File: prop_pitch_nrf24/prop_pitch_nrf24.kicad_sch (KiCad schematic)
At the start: 54 parts, among them J1 LOAD1, J2 LOAD2, J3 AVR-UPDI-6, J4 SERVO2, J5 SERVO1, J6 SERIAL, Q1 MMSS8550, U1 ATtiny1616-M, U2 HX711, U3 TPS563208DDCR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

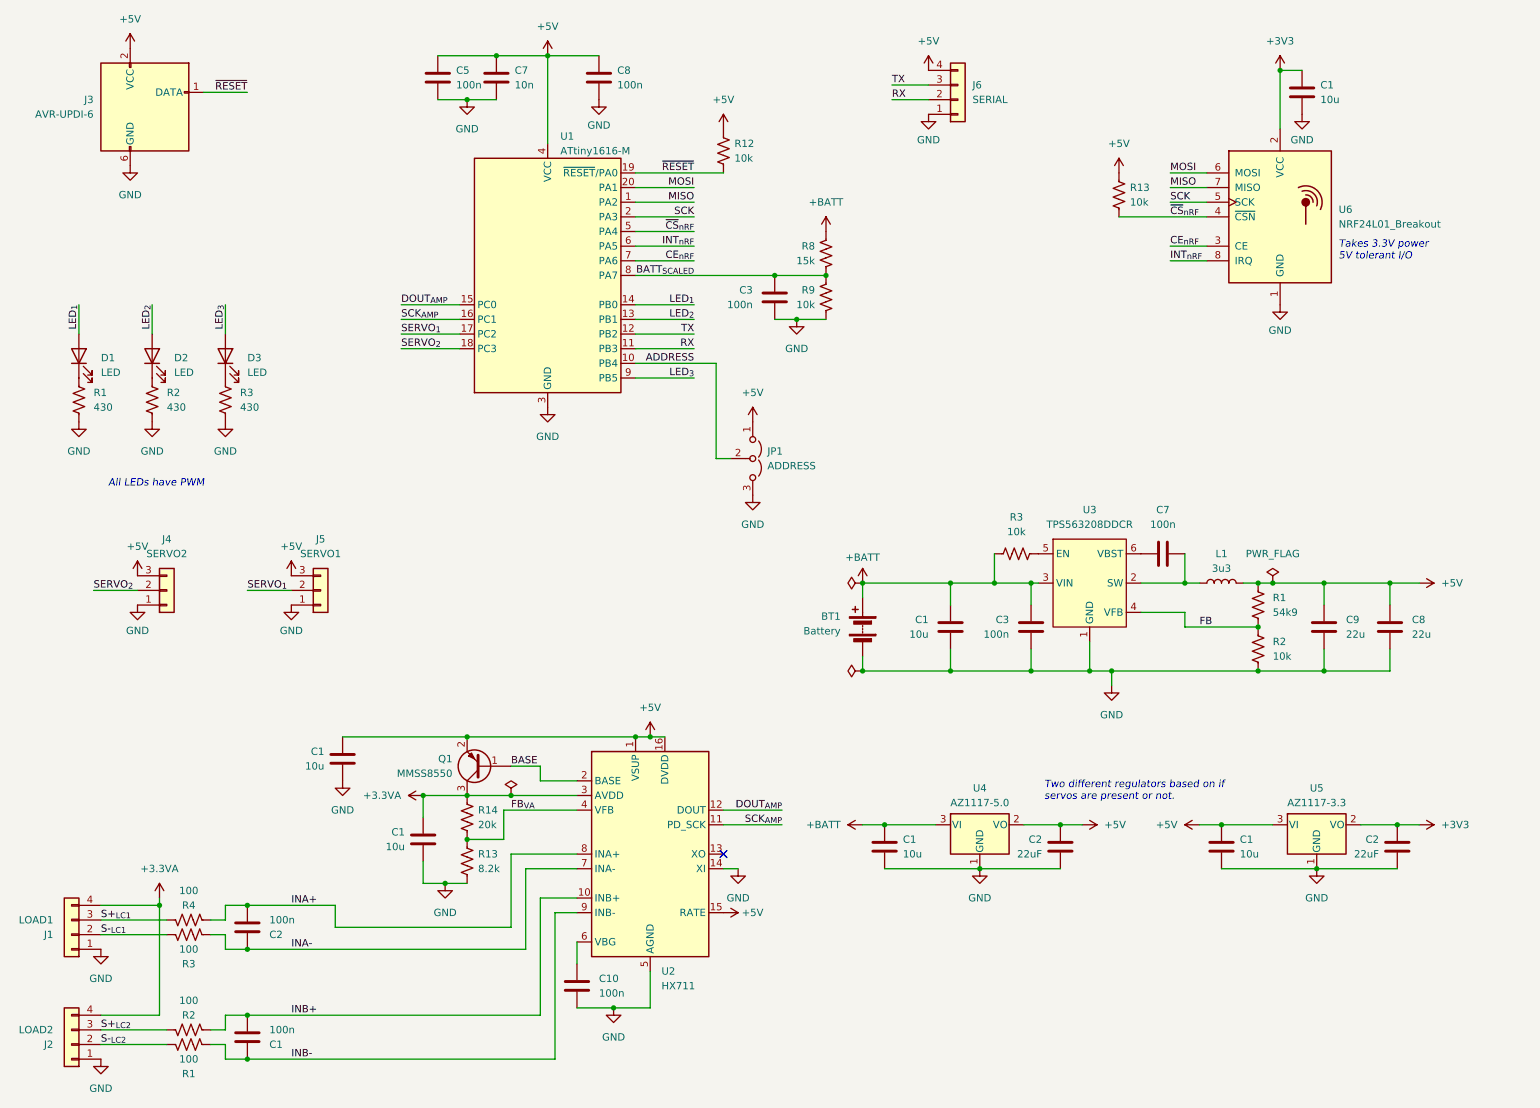
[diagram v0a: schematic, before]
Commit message: Finished first version of prop control layout
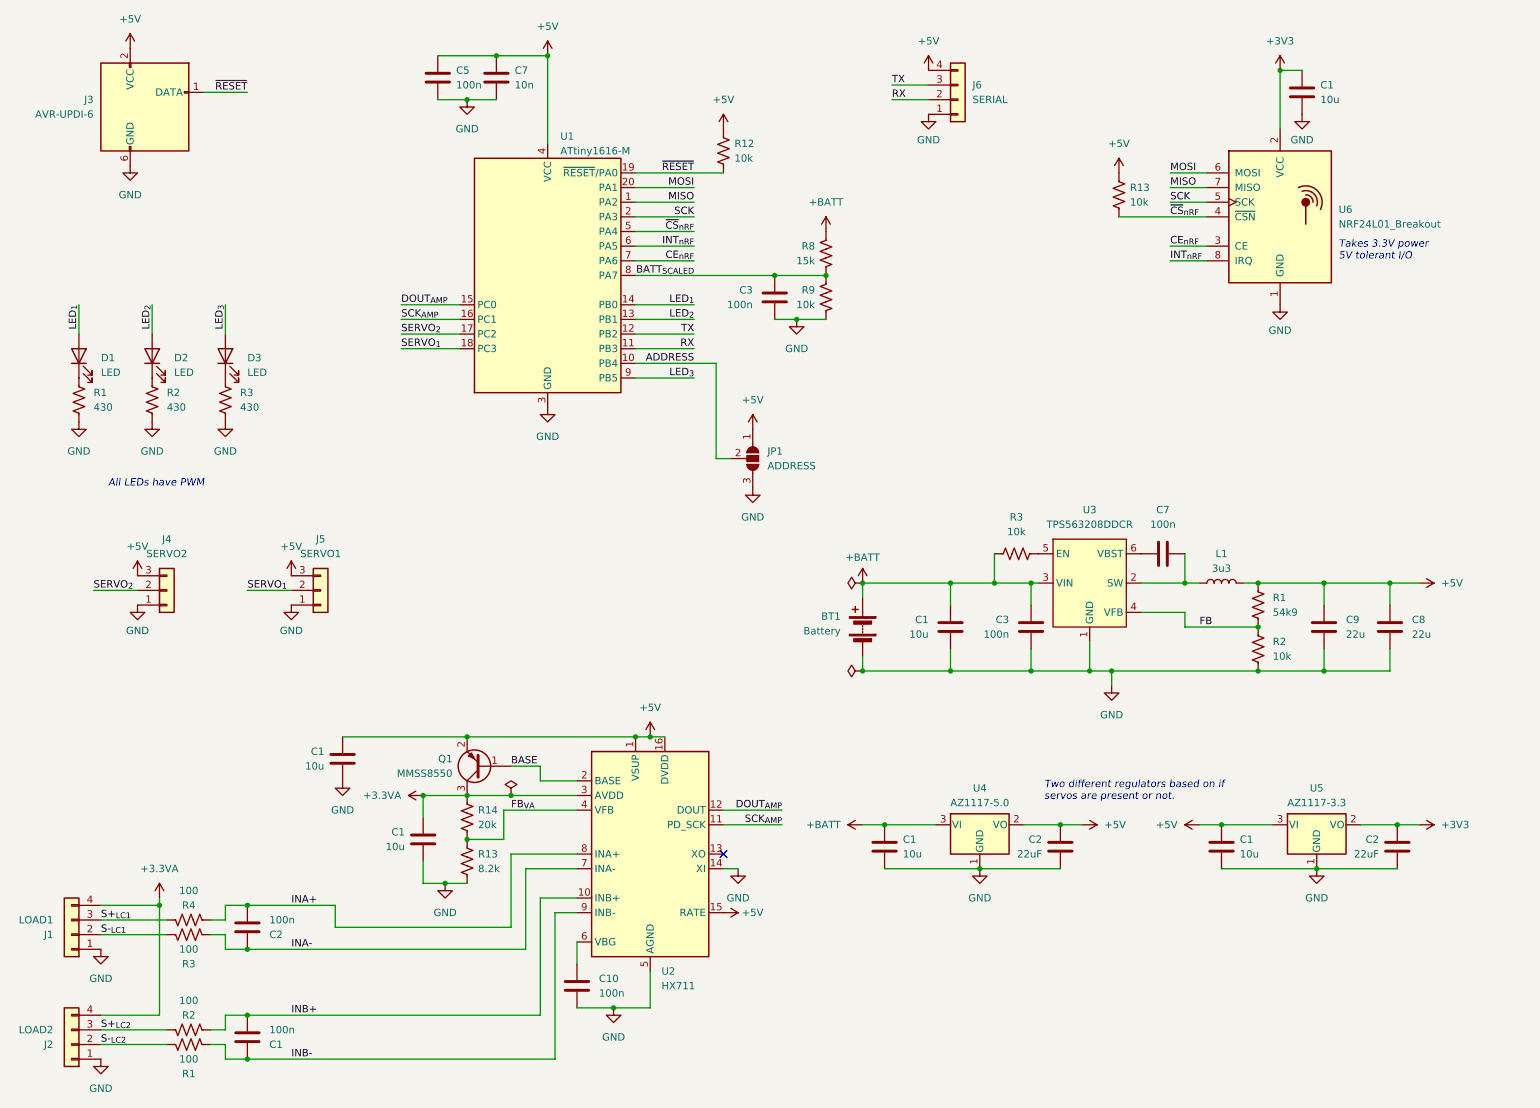
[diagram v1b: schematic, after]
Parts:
- removed C8: 100n, Capacitor_SMD:C_0603_1608Metric, symbol Device:C
- JP1: footprint Jumper:SolderJumper-3_P1.3mm_Open_Pad1.0x1.5mm_NumberLabels -> Jumper:SolderJumper-3_P1.3mm_Open_Pad1.0x1.5mm; symbol Jumper:Jumper_3_Open -> Jumper:SolderJumper_3_Open
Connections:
- net SERVO_{1}: now also U1.18 (PC3); no longer U1.17 (PC2)
- net SERVO_{2}: now also U1.17 (PC2); no longer U1.18 (PC3)
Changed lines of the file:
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@@
   (junction (at 100.33 151.13) (diameter 0) (color 0 0 0 0)
   )
-  (junction (at 232.41 114.3) (diameter 0) (color 0 0 0 0)
-  )
   (junction (at 241.3 129.54) (diameter 0) (color 0 0 0 0)
   )
@@
     (stroke (width 0) (type default))
   )
-  (wire (pts (xy 229.87 114.3) (xy 232.41 114.3))
+  (wire (pts (xy 229.87 114.3) (xy 241.3 114.3))
     (stroke (width 0) (type default))
   )
@@
     (stroke (width 0) (type default))
   )
-  (wire (pts (xy 232.41 114.3) (xy 241.3 114.3))
-    (stroke (width 0) (type default))
-  )
   (wire (pts (xy 121.92 76.2) (xy 135.89 76.2))
     (stroke (width 0) (type default))
@@
     (stroke (width 0) (type default))
   )
-  (wire (pts (xy 106.68 22.86) (xy 115.57 22.86))
-    (stroke (width 0) (type default))
-  )
   (text_box "Two different regulators based on if servos are present or not."
     (at 191.77 147.32 0) (size 38.735 5.08)
@@
     (effects (font (size 1.27 1.27)) (justify right bottom))
   )
-  (label "SERVO_{1}" (at 81.28 71.12 0) (fields_autoplaced)
-    (effects (font (size 1.27 1.27)) (justify left bottom))
-  )
   (label "S-_{LC1}" (at 29.21 175.26 0) (fields_autoplaced)
     (effects (font (size 1.27 1.27)) (justify left bottom))
@@
     (effects (font (size 1.27 1.27)) (justify left bottom))
   )
-  (label "FB" (at 219.71 121.92 0) (fields_autoplaced)
+  (label "SERVO_{2}" (at 81.28 71.12 0) (fields_autoplaced)
     (effects (font (size 1.27 1.27)) (justify left bottom))
   )
-  (label "SERVO_{2}" (at 81.28 73.66 0) (fields_autoplaced)
+  (label "FB" (at 219.71 121.92 0) (fields_autoplaced)
     (effects (font (size 1.27 1.27)) (justify left bottom))
   )
@@
     (effects (font (size 1.27 1.27)) (justify left bottom))
   )
+  (label "SERVO_{1}" (at 81.28 73.66 0) (fields_autoplaced)
+    (effects (font (size 1.27 1.27)) (justify left bottom))
+  )
   (label "~{RESET}" (at 54.61 29.21 180) (fields_autoplaced)
     (effects (font (size 1.27 1.27)) (justify right bottom))
@@
     )
   )
-  (symbol (lib_id "Device:C") (at 115.57 26.67 0) (unit 1)
-    (in_bom yes) (on_board yes) (dnp no) (fields_autoplaced)
-    (property "Reference" "C8" (at 118.745 25.4 0)
-      (effects (font (size 1.27 1.27)) (justify left))
-    )
-    (property "Value" "100n" (at 118.745 27.94 0)
-      (effects (font (size 1.27 1.27)) (justify left))
-    )
-    (property "Footprint" "Capacitor_SMD:C_0603_1608Metric" (at 116.5352 30.48 0)
-      (effects (font (size 1.27 1.27)) hide)
-    )
-    (property "Datasheet" "~" (at 115.57 26.67 0)
-      (effects (font (size 1.27 1.27)) hide)
-    )
-    (pin "1")
-    (pin "2")
-    (instances
-      (project "prop_pitch_nrf24"
-        (path "/a5c1c062-6aa5-4755-b14a-86c74d90c376"
-          (reference "C8") (unit 1)
-        )
-      )
-    )
-  )
   (symbol (lib_id "Device:C") (at 213.36 109.22 90) (unit 1)
     (in_bom yes) (on_board yes) (dnp no) (fields_autoplaced)
@@
     )
   )
-  (symbol (lib_id "power:+5V") (at 142.24 86.36 0) (unit 1)
+  (symbol (lib_id "power:+5V") (at 142.24 87.63 0) (unit 1)
     (in_bom yes) (on_board yes) (dnp no) (fields_autoplaced)
-    (property "Reference" "#PWR048" (at 142.24 90.17 0)
+    (property "Reference" "#PWR048" (at 142.24 91.44 0)
       (effects (font (size 1.27 1.27)) hide)
     )
-    (property "Value" "+5V" (at 142.24 81.28 0)
+    (property "Value" "+5V" (at 142.24 82.55 0)
       (effects (font (size 1.27 1.27)))
     )
-    (property "Footprint" "" (at 142.24 86.36 0)
+    (property "Footprint" "" (at 142.24 87.63 0)
       (effects (font (size 1.27 1.27)) hide)
     )
-    (property "Datasheet" "" (at 142.24 86.36 0)
+    (property "Datasheet" "" (at 142.24 87.63 0)
       (effects (font (size 1.27 1.27)) hide)
     )
@@
     )
   )
-  (symbol (lib_id "Jumper:Jumper_3_Open") (at 142.24 92.71 270) (unit 1)
+  (symbol (lib_id "Jumper:SolderJumper_3_Open") (at 142.24 92.71 270) (unit 1)
     (in_bom yes) (on_board yes) (dnp no) (fields_autoplaced)
     (property "Reference" "JP1" (at 144.78 91.44 90)
@@
       (effects (font (size 1.27 1.27)) (justify left))
     )
-    (property "Footprint" "Jumper:SolderJumper-3_P1.3mm_Open_Pad1.0x1.5mm_NumberLabels" (at 142.24 92.71 0)
+    (property "Footprint" "Jumper:SolderJumper-3_P1.3mm_Open_Pad1.0x1.5mm" (at 142.24 92.71 0)
       (effects (font (size 1.27 1.27)) hide)
     )
@@
     )
   )
-  (symbol (lib_id "power:GND") (at 142.24 99.06 0) (mirror y) (unit 1)
+  (symbol (lib_id "power:GND") (at 142.24 97.79 0) (mirror y) (unit 1)
     (in_bom yes) (on_board yes) (dnp no) (fields_autoplaced)
-    (property "Reference" "#PWR047" (at 142.24 105.41 0)
+    (property "Reference" "#PWR047" (at 142.24 104.14 0)
       (effects (font (size 1.27 1.27)) hide)
     )
-    (property "Value" "GND" (at 142.24 104.14 0)
+    (property "Value" "GND" (at 142.24 102.87 0)
       (effects (font (size 1.27 1.27)))
     )
-    (property "Footprint" "" (at 142.24 99.06 0)
+    (property "Footprint" "" (at 142.24 97.79 0)
       (effects (font (size 1.27 1.27)) hide)
     )
-    (property "Datasheet" "" (at 142.24 99.06 0)
+    (property "Datasheet" "" (at 142.24 97.79 0)
       (effects (font (size 1.27 1.27)) hide)
     )
@@
     )
   )
-  (symbol (lib_id "power:PWR_FLAG") (at 232.41 114.3 0) (unit 1)
-    (in_bom yes) (on_board yes) (dnp no) (fields_autoplaced)
-    (property "Reference" "#FLG04" (at 232.41 112.395 0)
-      (effects (font (size 1.27 1.27)) hide)
-    )
-    (property "Value" "PWR_FLAG" (at 232.41 109.22 0)
-      (effects (font (size 1.27 1.27)))
-    )
-    (property "Footprint" "" (at 232.41 114.3 0)
-      (effects (font (size 1.27 1.27)) hide)
-    )
-    (property "Datasheet" "~" (at 232.41 114.3 0)
-      (effects (font (size 1.27 1.27)) hide)
-    )
-    (pin "1")
-    (instances
-      (project "prop_pitch_nrf24"
-        (path "/a5c1c062-6aa5-4755-b14a-86c74d90c376"
-          (reference "#FLG04") (unit 1)
-        )
-      )
-      (project "downlink_board"
-        (path "/e63e39d7-6ac0-4ffd-8aa3-1841a4541b55"
-          (reference "#FLG05") (unit 1)
-        )
-      )
-    )
-  )
   (symbol (lib_id "Device:R_US") (at 92.71 162.56 0) (unit 1)
     (in_bom yes) (on_board yes) (dnp no) (fields_autoplaced)
@@
         )
       )
-    )
-  )
-  (symbol (lib_id "power:GND") (at 115.57 30.48 0) (unit 1)
-    (in_bom yes) (on_board yes) (dnp no) (fields_autoplaced)
-    (property "Reference" "#PWR021" (at 115.57 36.83 0)
-      (effects (font (size 1.27 1.27)) hide)
-    )
-    (property "Value" "GND" (at 115.57 34.925 0)
-      (effects (font (size 1.27 1.27)))
-    )
-    (property "Footprint" "" (at 115.57 30.48 0)
-      (effects (font (size 1.27 1.27)) hide)
-    )
-    (property "Datasheet" "" (at 115.57 30.48 0)
-      (effects (font (size 1.27 1.27)) hide)
-    )
-    (pin "1")
-    (instances
-      (project "prop_pitch_nrf24"
-        (path "/a5c1c062-6aa5-4755-b14a-86c74d90c376"
-          (reference "#PWR021") (unit 1)
-        )
-      )

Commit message: Cleaned up nRF schematic
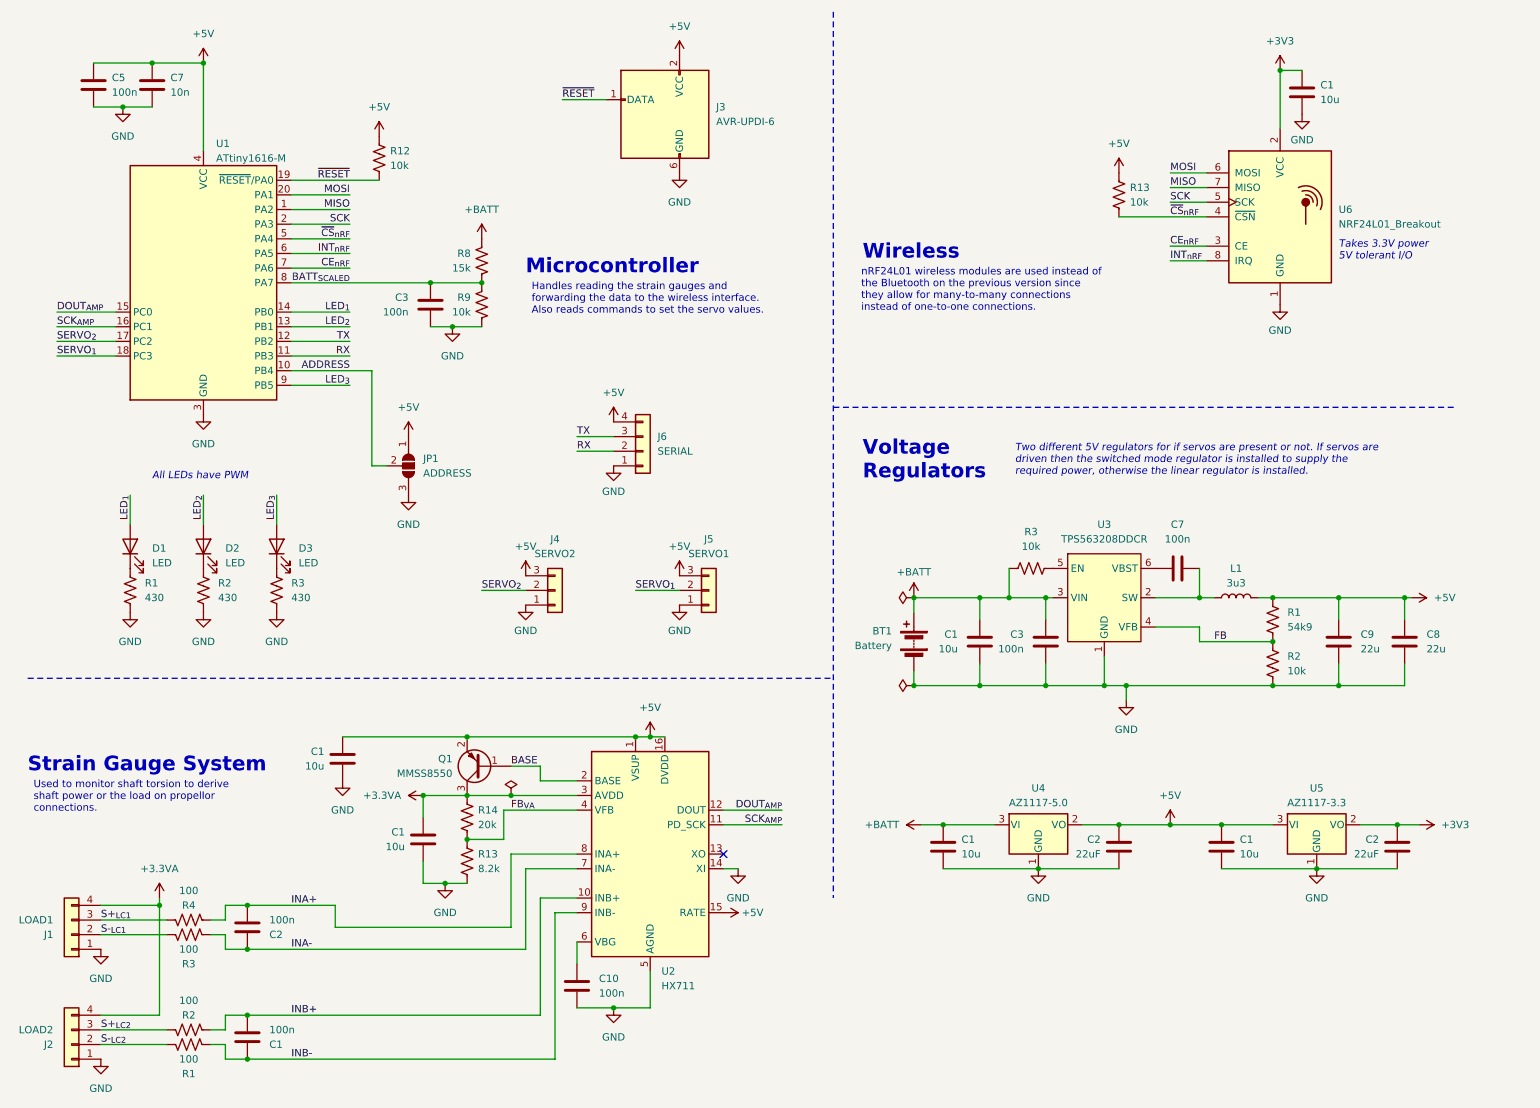
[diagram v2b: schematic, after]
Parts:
- JP1: now left out of the parts list
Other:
- note added: "Microcontroller"
- note added: "Strain Gauge System"
- note added: "Voltage Regulators"
- note added: "Wireless"
- moved on the sheet: BT1, C1, C2, C3, C5, C7, C8, C9, D1, D2, D3, J3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

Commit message: Touched up values for BOMs
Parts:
- C2: value 22uF -> 22u
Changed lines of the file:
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@@
   (symbol (lib_id "Device:C") (at 254 160.02 180) (unit 1)
     (in_bom yes) (on_board yes) (dnp no) (fields_autoplaced)
-    (property "Reference" "C2" (at 250.825 158.75 0)
-      (effects (font (size 1.27 1.27)) (justify left))
-    )
-    (property "Value" "22uF" (at 250.825 161.29 0)
-      (effects (font (size 1.27 1.27)) (justify left))
+    (property "Reference" "C2" (at 257.81 158.75 0)
+      (effects (font (size 1.27 1.27)) (justify right))
+    )
+    (property "Value" "22u" (at 257.81 161.29 0)
+      (effects (font (size 1.27 1.27)) (justify right))
     )
     (property "Footprint" "Capacitor_SMD:C_0805_2012Metric" (at 253.0348 156.21 0)
@@
   (symbol (lib_id "Device:C") (at 205.74 160.02 180) (unit 1)
     (in_bom yes) (on_board yes) (dnp no) (fields_autoplaced)
-    (property "Reference" "C2" (at 202.565 158.75 0)
-      (effects (font (size 1.27 1.27)) (justify left))
-    )
-    (property "Value" "22uF" (at 202.565 161.29 0)
-      (effects (font (size 1.27 1.27)) (justify left))
+    (property "Reference" "C2" (at 209.55 158.75 0)
+      (effects (font (size 1.27 1.27)) (justify right))
+    )
+    (property "Value" "22u" (at 209.55 161.29 0)
+      (effects (font (size 1.27 1.27)) (justify right))
     )
     (property "Footprint" "Capacitor_SMD:C_0805_2012Metric" (at 204.7748 156.21 0)
